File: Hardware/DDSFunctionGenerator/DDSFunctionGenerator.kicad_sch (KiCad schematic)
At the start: 0 parts

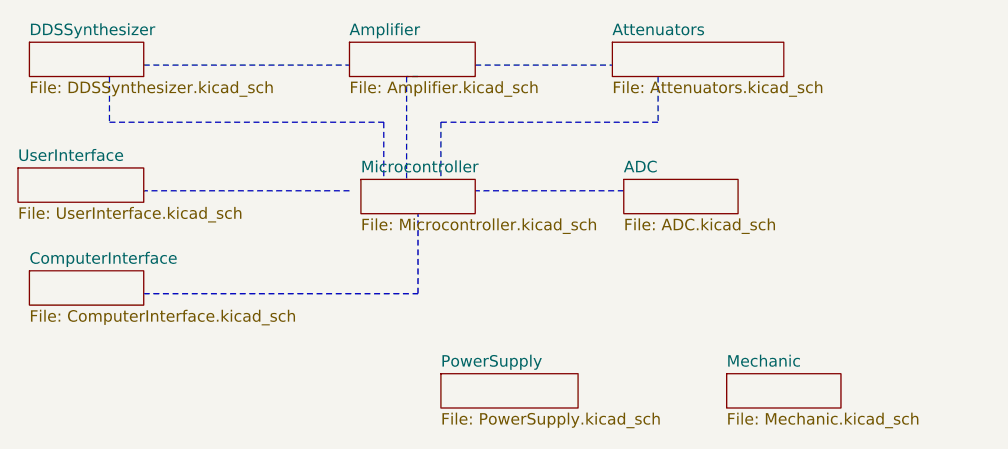
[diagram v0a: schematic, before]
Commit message: move to raspbbery pico, first draft
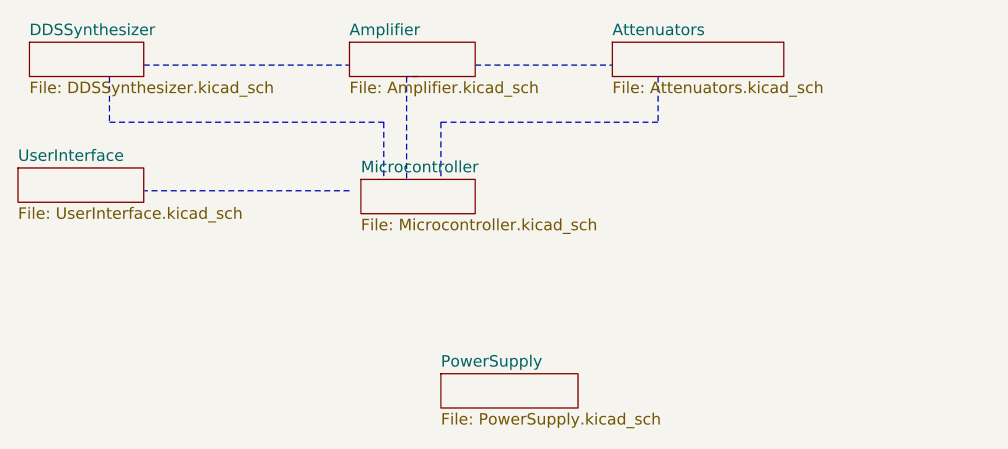
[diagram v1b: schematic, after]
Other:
- removed sheet ADC
- removed sheet ComputerInterface
- removed sheet Mechanic
